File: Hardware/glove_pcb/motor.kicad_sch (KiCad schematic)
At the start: 11 parts, among them J1 Conn_01x02, U3 DRV8876PWPR

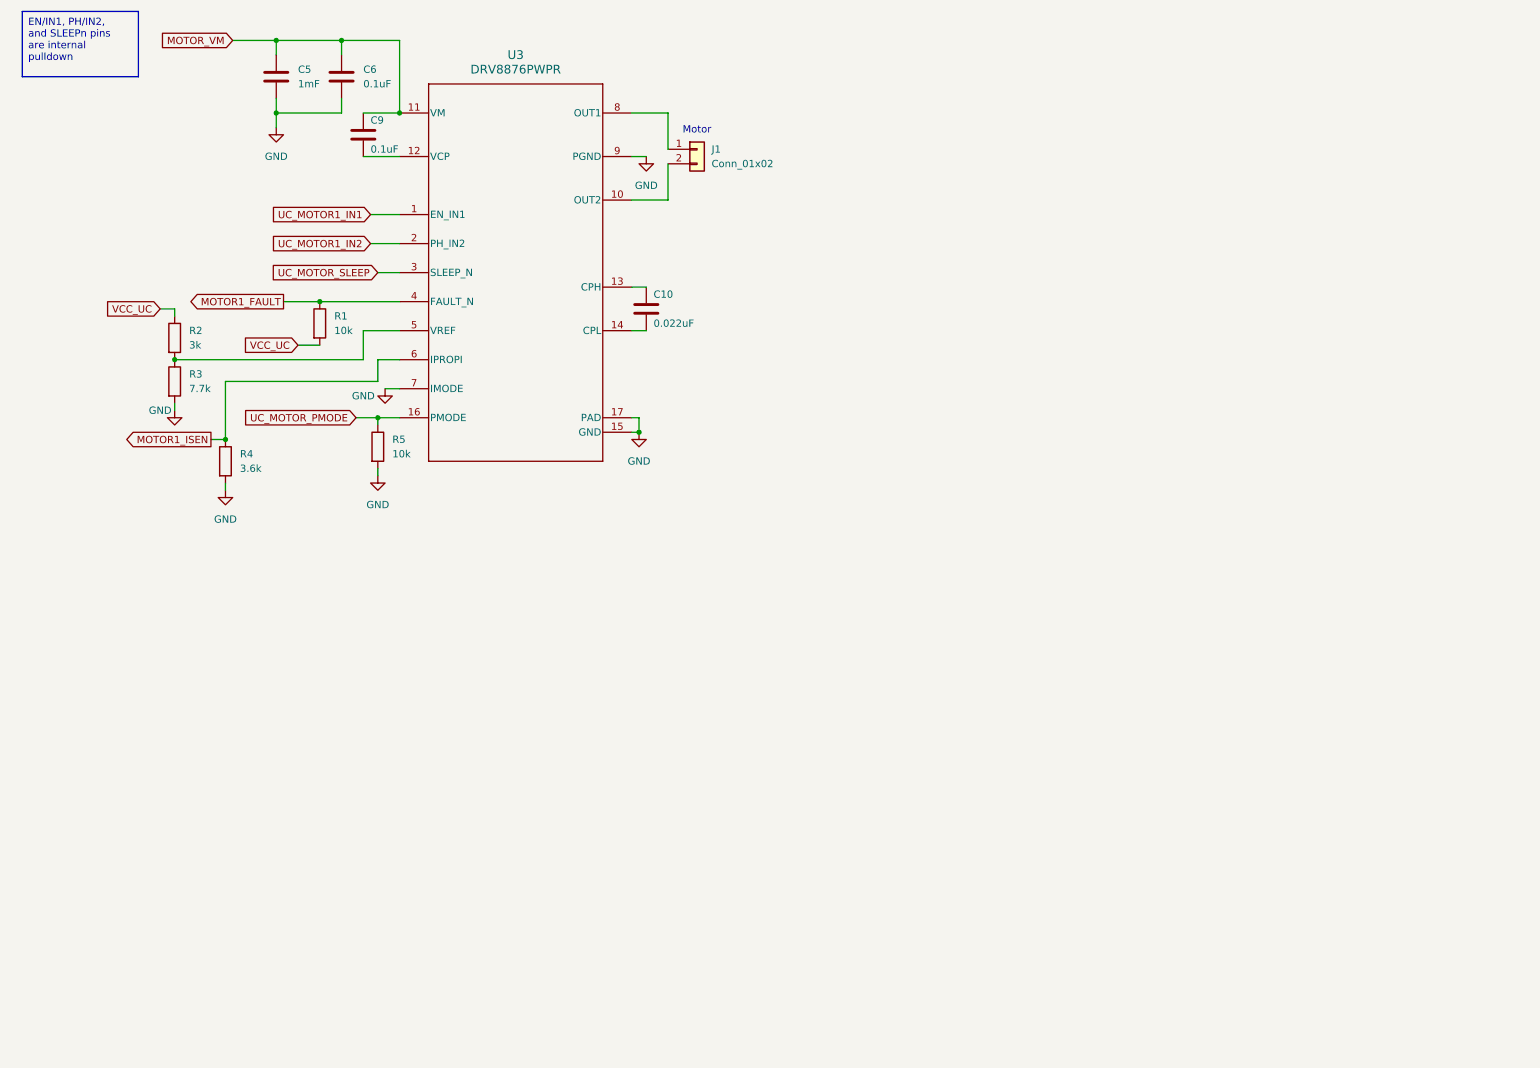
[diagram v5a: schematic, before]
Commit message: Finish schematic
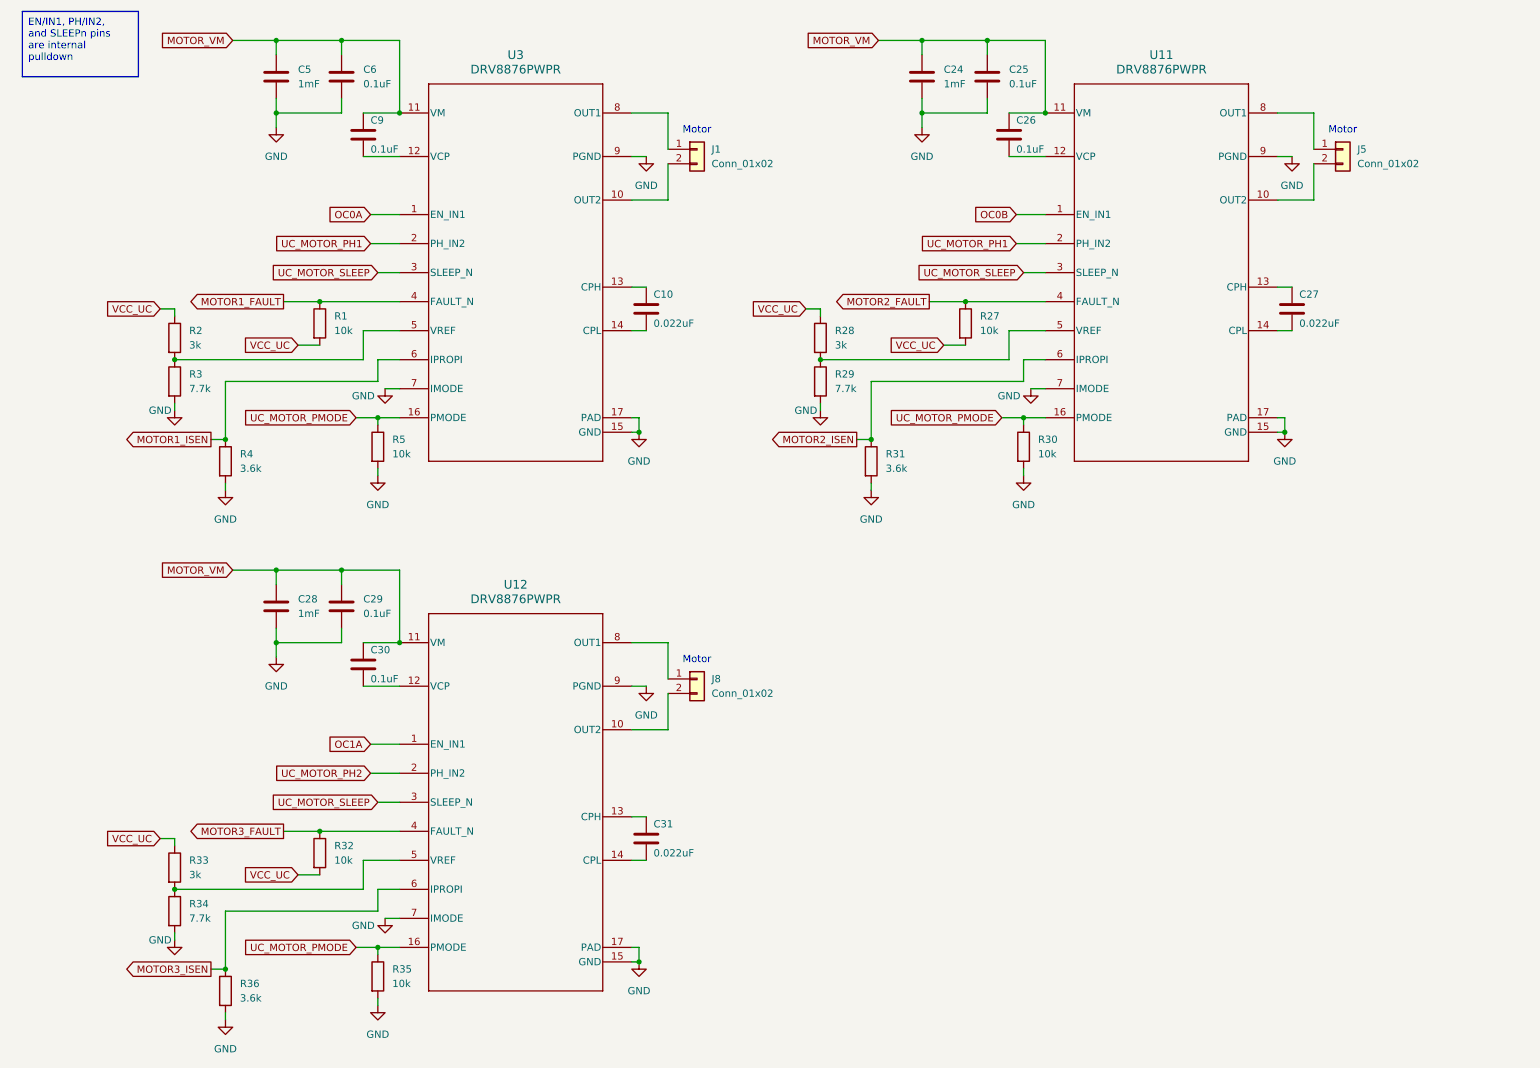
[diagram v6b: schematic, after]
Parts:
- added C24, C28: 1mF, symbol Device:C
- added C25, C26, C29, C30: 0.1uF, symbol Device:C
- added C27, C31: 0.022uF, symbol Device:C
- added J5, J8: Conn_01x02, symbol Connector_Generic:Conn_01x02
- added R27, R30, R32, R35: 10k, symbol Device:R
- added R28, R33: 3k, symbol Device:R
- added R29, R34: 7.7k, symbol Device:R
- added R31, R36: 3.6k, symbol Device:R
- added U11, U12: DRV8876PWPR, PWP0016J_N, symbol Glove_Symbols:DRV8876PWPR
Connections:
- net GND: now also C24.2, C25.2, C28.2, C29.2, R29.2, R30.2, R31.2, R34.2, R35.2, R36.2, U11.15 (GND), U11.17 (PAD), U11.7 (IMODE), U11.9 (PGND), U12.15 (GND), U12.17 (PAD), U12.7 (IMODE), U12.9 (PGND)
- net MOTOR_VM: now also C24.1, C25.1, C26.1, C28.1, C29.1, C30.1, U11.11 (VM), U12.11 (VM)
- net UC_MOTOR_PMODE: now also R30.1, R35.1, U11.16 (PMODE), U12.16 (PMODE)
- net UC_MOTOR_SLEEP: now also U11.3 (SLEEP_N), U12.3 (SLEEP_N)
- net VCC_UC: now also R27.2, R28.1, R32.2, R33.1
- net UC_MOTOR1_IN1 renamed OC0A
- net UC_MOTOR1_IN2 renamed UC_MOTOR_PH1
- net UC_MOTOR_PH1: now also U11.2 (PH_IN2)
- new net: C30.2, U12.12 (VCP)
- new net: R33.2, R34.1, U12.5 (VREF)
- new net: J5.2 (Pin_2), U11.10 (OUT2)
- new net: C26.2, U11.12 (VCP)
- new net: C27.1, U11.13 (CPH)
- new net: C27.2, U11.14 (CPL)
- new net: R28.2, R29.1, U11.5 (VREF)
- new net: J5.1 (Pin_1), U11.8 (OUT1)
- new net: J8.1 (Pin_1), U12.8 (OUT1)
- new net: J8.2 (Pin_2), U12.10 (OUT2)
- new net: C31.1, U12.13 (CPH)
- new net: C31.2, U12.14 (CPL)
- new net MOTOR2_FAULT: R27.1, U11.4 (FAULT_N)
- new net MOTOR2_ISEN: R31.1, U11.6 (IPROPI)
- new net MOTOR3_FAULT: R32.1, U12.4 (FAULT_N)
- new net MOTOR3_ISEN: R36.1, U12.6 (IPROPI)
- new net OC0B: U11.1 (EN_IN1)
- new net OC1A: U12.1 (EN_IN1)
- new net UC_MOTOR_PH2: U12.2 (PH_IN2)

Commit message: Add titles to pages and reannotate
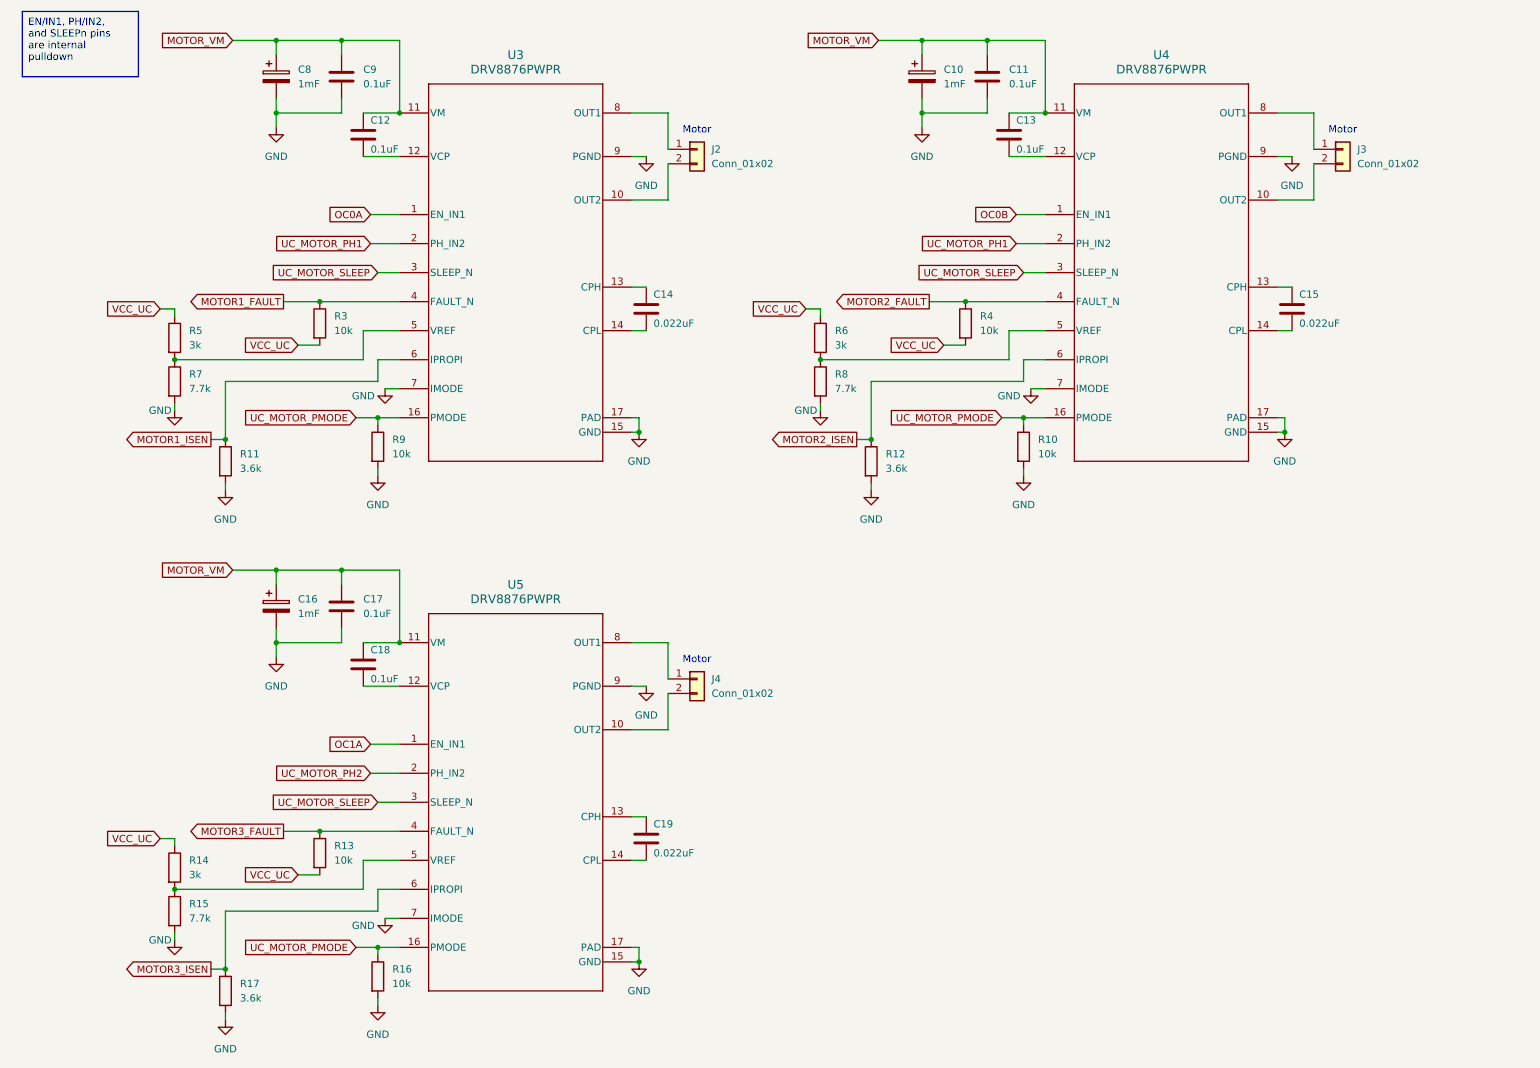
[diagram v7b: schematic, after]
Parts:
- C10: renamed from C24; symbol Device:C -> Device:C_Polarized
- C16: renamed from C28; symbol Device:C -> Device:C_Polarized
- C8: renamed from C5; symbol Device:C -> Device:C_Polarized
- renumbered C25 to C11, C9 to C12, C26 to C13, C10 to C14, C27 to C15, C29 to C17, C30 to C18, C31 to C19, C6 to C9, J1 to J2, J5 to J3, J8 to J4, R30 to R10, R4 to R11, R31 to R12, R32 to R13, R33 to R14, R34 to R15, R35 to R16, R36 to R17, R1 to R3, R27 to R4, R2 to R5, R28 to R6, R3 to R7, R29 to R8, R5 to R9, U11 to U4, U12 to U5
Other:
- company: (none) -> COEN 490 Team 15
- title: (none) -> Motor Drivers (1/2)

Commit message: Finalize schematic for real this time
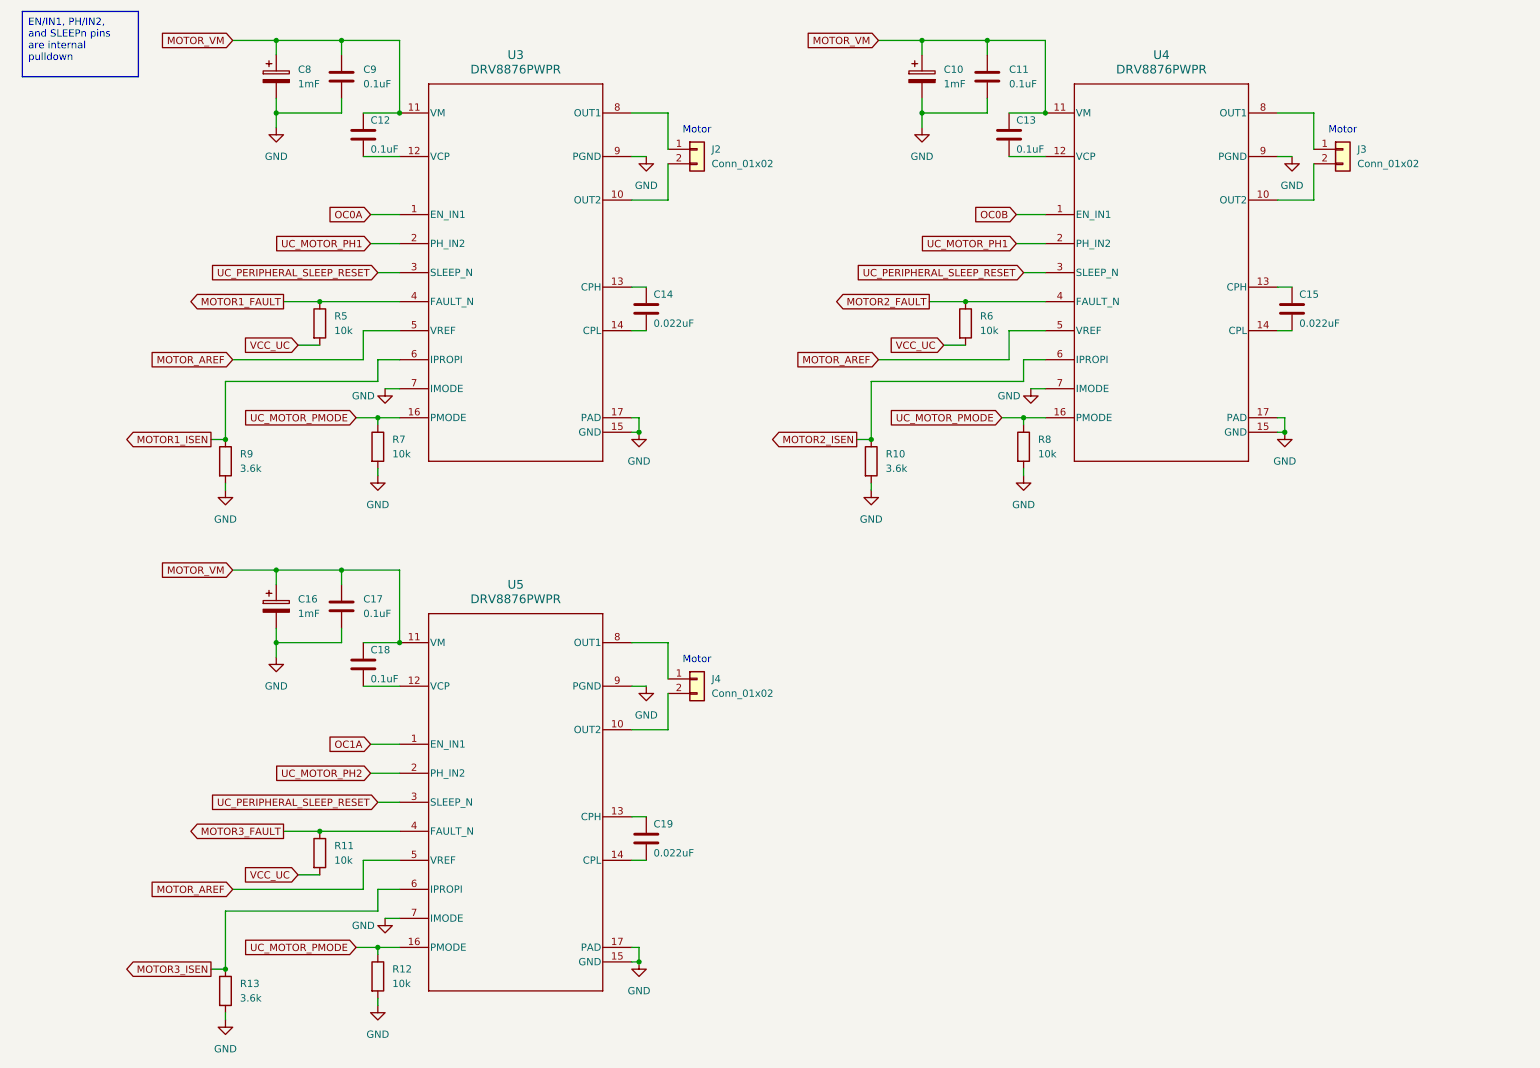
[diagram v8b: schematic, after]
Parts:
- removed R14, R5, R6: 3k, symbol Device:R
- removed R15, R7, R8: 7.7k, symbol Device:R
- renumbered R12 to R10, R13 to R11, R16 to R12, R17 to R13, R3 to R5, R4 to R6, R9 to R7, R10 to R8, R11 to R9
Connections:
- net MOTOR_AREF: now reaches U5.5 (VREF)
- net MOTOR_AREF: now also U3.5 (VREF), U4.5 (VREF)
- net UC_MOTOR_SLEEP renamed UC_PERIPHERAL_SLEEP_RESET
